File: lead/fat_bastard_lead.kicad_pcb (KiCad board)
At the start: 2 copper layers, 180 x 35 mm, 38 parts, among them J1 LD_12V, J2 LD_IN, J3 LD_GAIN, J4 LD_OUT, J5 HT_IN, U1 ECC83, U2 ECC83

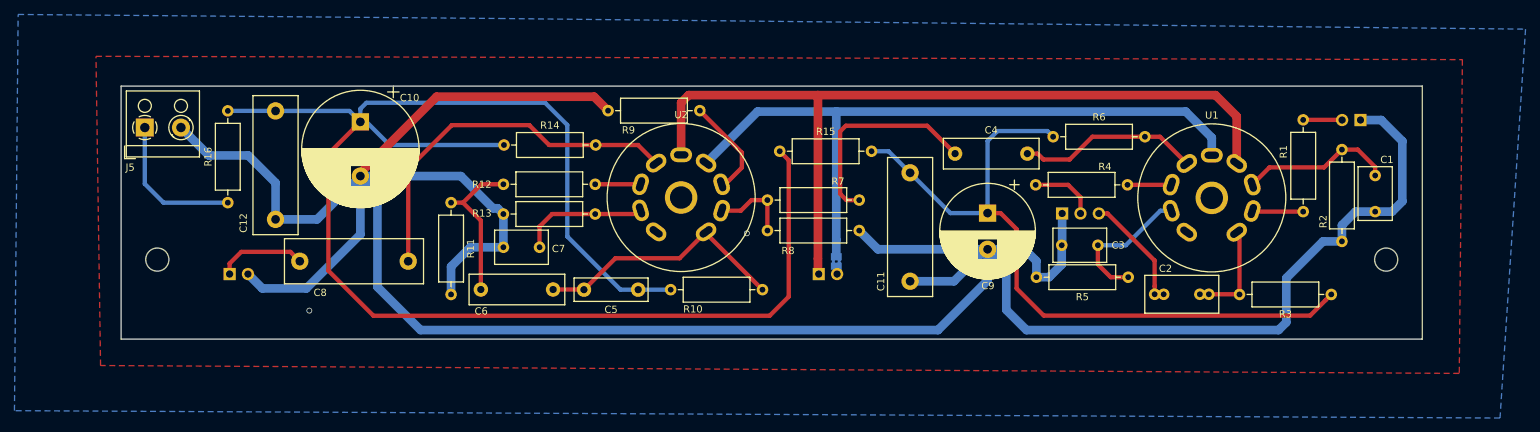
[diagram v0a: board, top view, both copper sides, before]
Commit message: Add license (CERN OHL v.1.2)
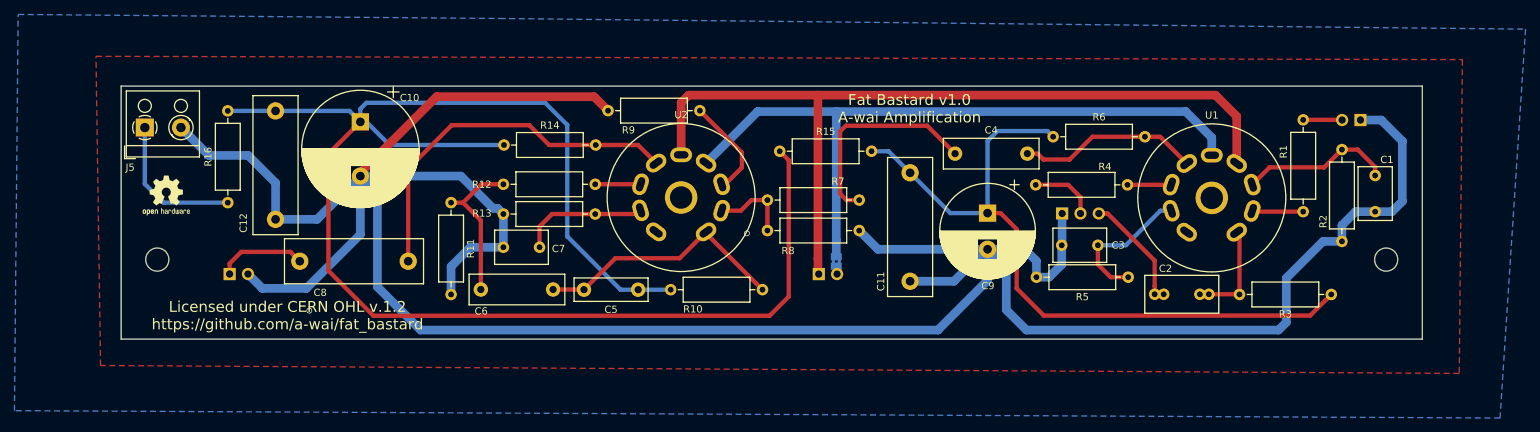
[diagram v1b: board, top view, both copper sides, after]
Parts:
- added REF**: OSHW-Logo2_7.3x6mm_SilkScreen, Symbol:OSHW-Logo2_7.3x6mm_SilkScreen, F.Cu at (66.2, 75.1)
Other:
- board text added: "Fat Bastard v1.0 A-wai Amplification"
- board text added: "Licensed under CERN OHL v.1.2 https://github.com/a-wai/fat_bastard"

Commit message: Improve tubes PCB & add tubes 3D models
Small changes were made to the lead PCB in order to avoid having solders
touching the main PCB.

Additionnally, the tubes footprints have been replaced to accomodate
PCB-mount tube sockets, and 3D models have been added for the tubes in
order to improve 3D rendering.
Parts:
- U1, U2: footprint Valve:Valve_ECC-83-2 -> ProjectLib:Valve_Noval-B9A_Belton-VT9-PT_Socket
- moved R9 12.5 mm to (127.6, 62.2)
- moved C2 5.75 mm to (197.3, 89.4)
- moved R14 4.22 mm to (108.7, 68.1)
- moved U1 3.86 mm to (217.0, 83.0), turned to 180 degrees
- moved U2 3.84 mm to (143.5, 83.0), turned to 180 degrees
- moved J2 3.66 mm to (234.1, 62.2)
- moved C1 3.66 mm to (236.1, 74.8)
- moved R1 3.66 mm to (226.2, 74.8)
- moved R2 3.66 mm to (231.5, 66.2)
- moved R6 3.08 mm to (185.9, 66.8)
- moved R4 2.99 mm to (196.3, 73.0)
- moved C3 2.86 mm to (187.5, 80.8)
- moved J3 2.79 mm to (187.6, 76.7)
- moved R10 2.45 mm to (138.4, 88.8)
- moved R3 2.31 mm to (229.7, 88.5)
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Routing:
- net GNDA: track 397.4 -> 373.4 mm
- net Net-(C4-Pad1): track 29.5 -> 14.1 mm
- net Net-(R9-Pad1): track 14.0 -> 25.3 mm
- net B+: track 215.4 -> 208.8 mm
- net +12V: track 116.9 -> 110.5 mm
- net /HT1: track 13.0 -> 19.4 mm
- net Net-(R17-Pad1): track 96.5 -> 90.2 mm
- net Net-(C7-Pad2): track 17.8 -> 13.0 mm
- net Net-(C2-Pad1): track 15.1 -> 19.3 mm
- net /HT4: track 51.8 -> 48.3 mm
- net Net-(R7-Pad2): track 11.2 -> 7.86 mm
- net /HT2: track 25.2 -> 22.2 mm
- net Net-(C3-Pad2): track 19.7 -> 17.1 mm
- net /HT3: track 35.7 -> 37.8 mm
- net C+: track 99.0 -> 101.0 mm
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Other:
- board text added: "Licensed under CERN OHL v.1.2 github.com/a-wai/fat_bastard"
- board text removed: "Licensed under CERN OHL v.1.2 https://github.com/a-wai/fat_bastard"

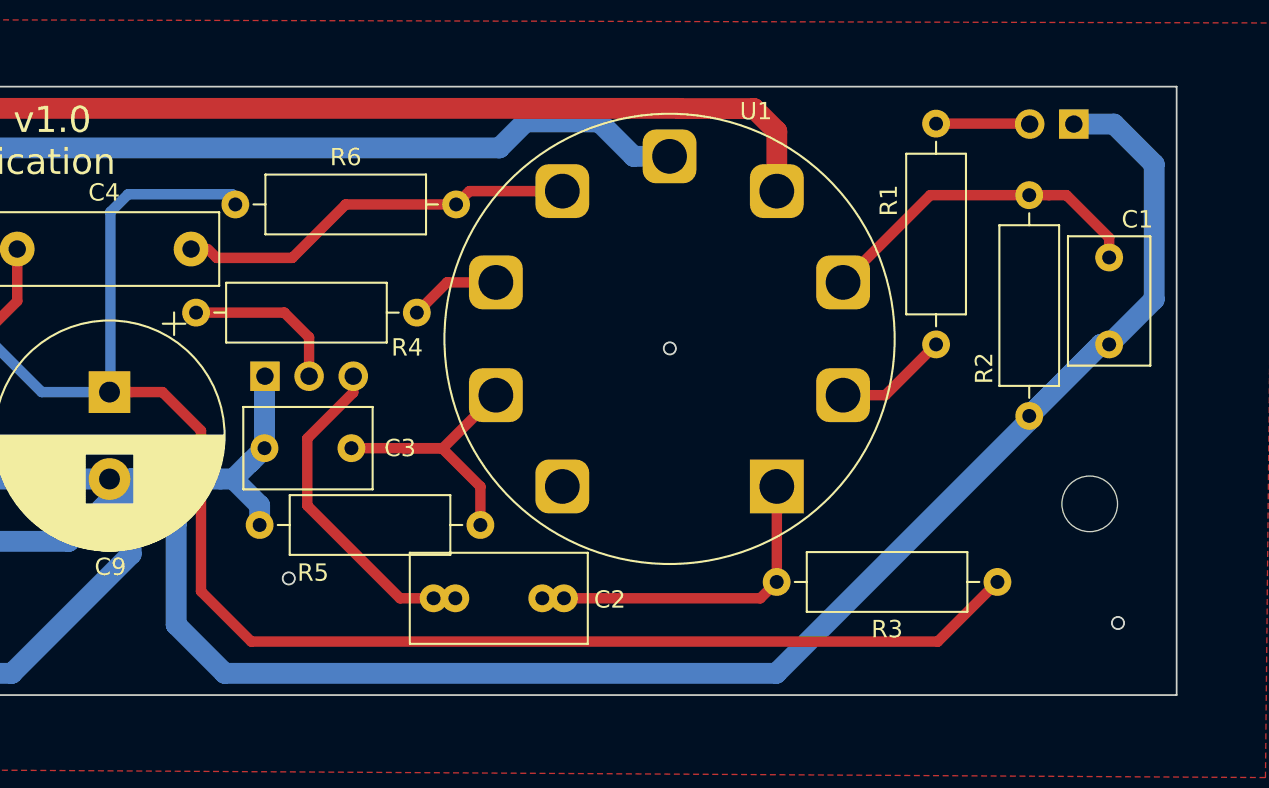
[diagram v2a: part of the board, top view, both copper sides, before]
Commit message: Add exclusion zones for mounting brackets
In order to avoid possible shortcuts, exclusion zones have been added to
the back side of the PCB, and a few components have been moved in order
to prevent unwanted contact.
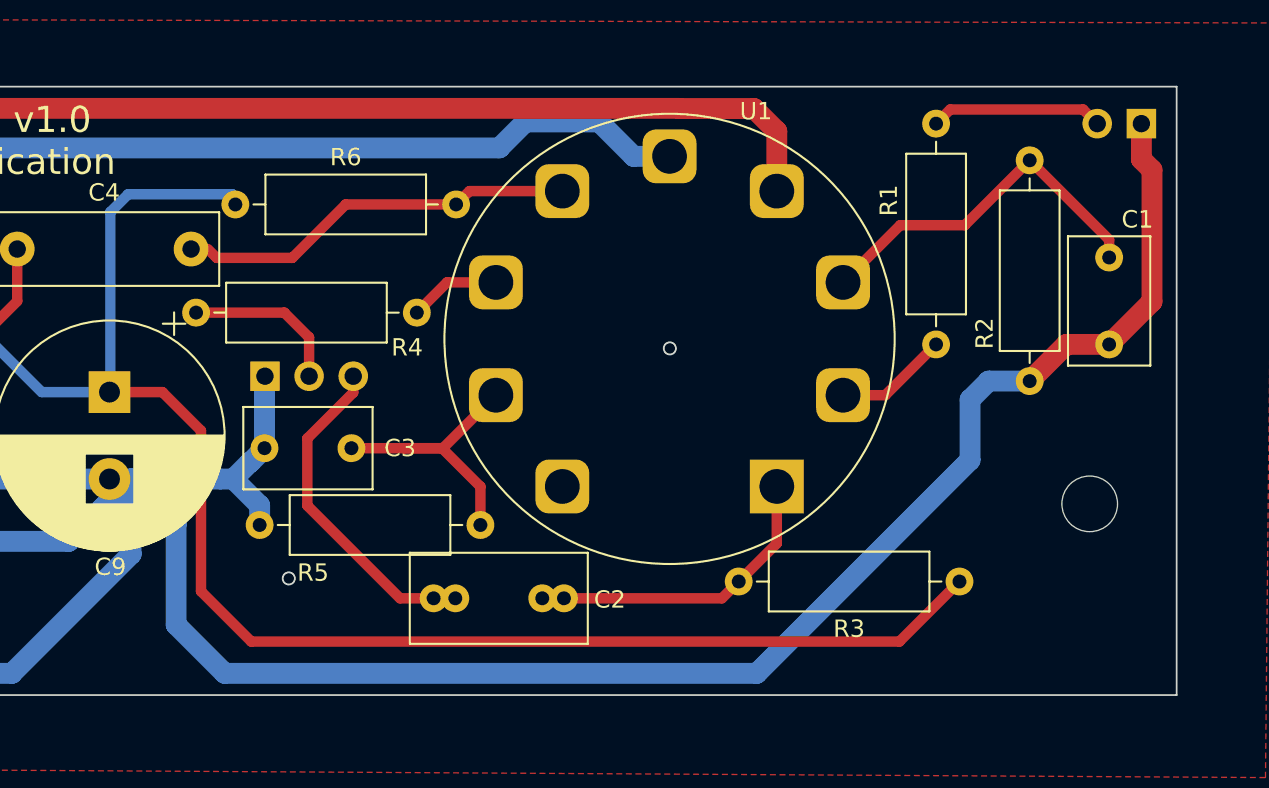
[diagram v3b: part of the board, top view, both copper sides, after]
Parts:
- moved J2 3.89 mm to (238.0, 62.1)
- moved R3 2.18 mm to (227.5, 88.5)
- moved R2 2.01 mm to (231.5, 64.2)
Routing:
- net Net-(J2-Pad2): track 5.40 -> 9.94 mm
- net C+: track 101.0 -> 98.9 mm
- net Net-(C1-Pad2): track 19.5 -> 21.1 mm
- net /HT1: track 19.4 -> 18.1 mm
- net GNDA: track 373.4 -> 372.2 mm
- net GND: vias 7 -> 6

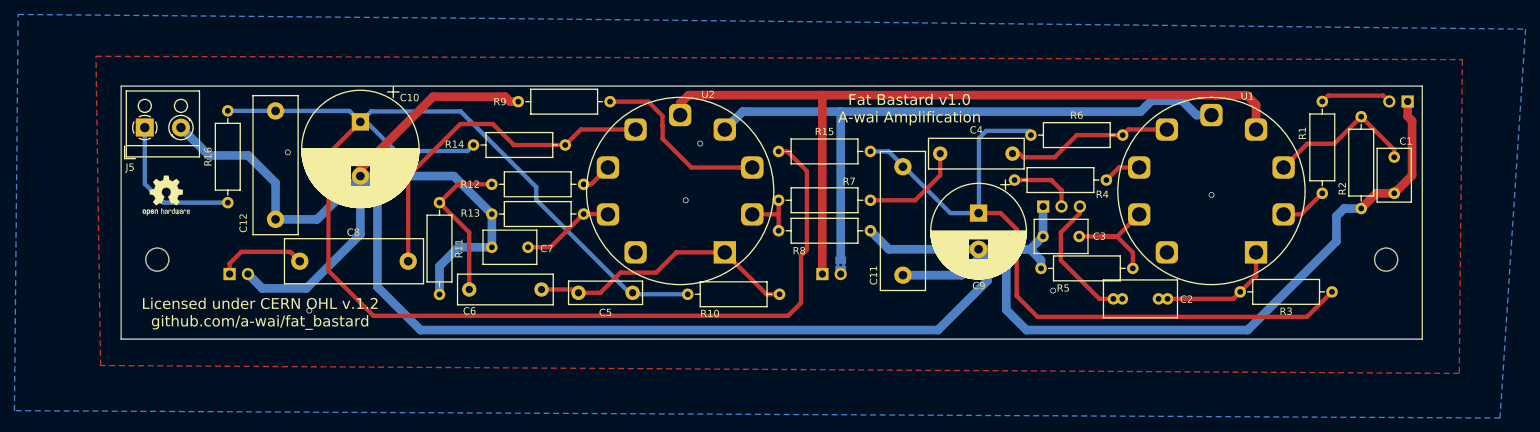
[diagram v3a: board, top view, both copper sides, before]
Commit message: [lead] Add small capacitor on last gain stage's anode
The schematics has too much treble for now, and must be used with the
Tone setting between 2 and 4/10. Adding this capacitor (300-500p, tune
to taste) gives a more full-bodied sound, and enables to use the Tone
control across a broader range.
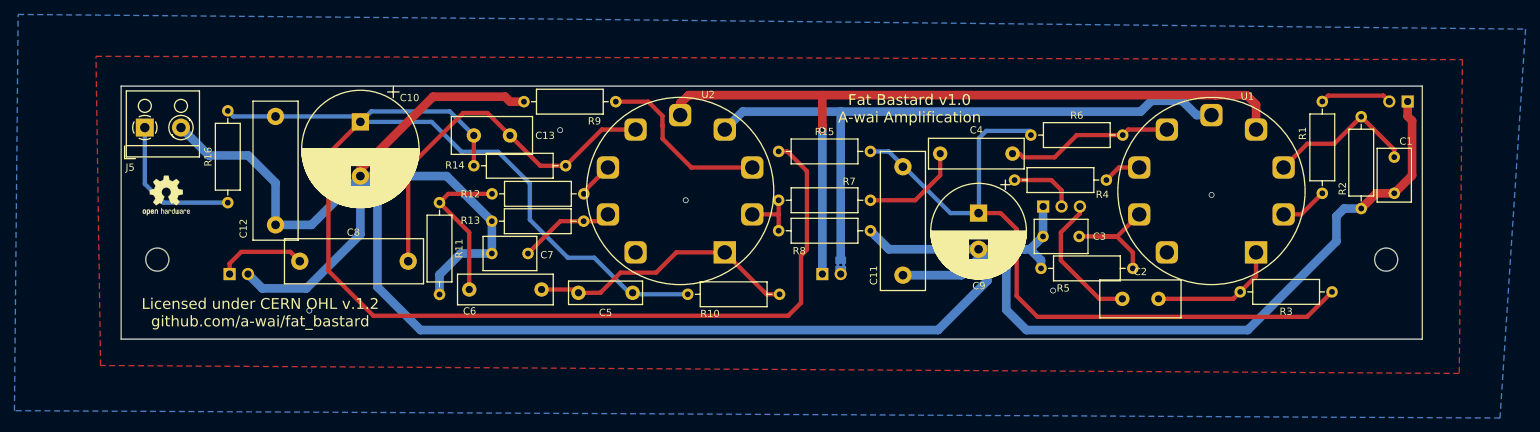
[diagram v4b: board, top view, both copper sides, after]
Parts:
- added C13: 500p, Capacitor_THT:C_Disc_D11.0mm_W5.0mm_P5.00mm, F.Cu at (108.8, 66.8)
- C2: footprint Capacitor_THT:C_Rect_L10.0mm_W5.0mm_P5.00mm_P7.50mm -> Capacitor_THT:C_Disc_D11.0mm_W5.0mm_P5.00mm
- moved R14 2.87 mm to (108.8, 71.0)
- moved R12 1.32 mm to (124.0, 74.9)
- moved C2 1.24 mm to (198.5, 89.4)
- moved R13 0.99 mm to (124.0, 78.7)
- moved C7 0.86 mm to (111.3, 83.2)
- moved R9 0.79 mm to (128.4, 62.2)
- moved C12 0.76 mm to (81.4, 79.2)
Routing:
- net B+: track 208.8 -> 213.7 mm
- net /HT4: track 48.3 -> 52.6 mm
- net GNDA: track 372.2 -> 373.3 mm
- net Net-(R9-Pad1): track 25.3 -> 24.5 mm
- net Net-(R12-Pad1): track 4.33 -> 5.03 mm
- net Net-(C6-Pad1): track 22.0 -> 21.5 mm
- net +12V: vias 0 -> 1
- net GND: vias 6 -> 5
